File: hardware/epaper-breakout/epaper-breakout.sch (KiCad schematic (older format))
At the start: 59 parts, among them J1 ED097OC4, J2 USB_B_Micro, J3 Conn_01x10, Q1 IRLML6402, SW1 RESET, SW2 BOOT, U1 LT1086-3.3, U2 LT1945, U3 L7915, U4 L7815, U5 ESP32-WROOM-32, U6 CH330N, U7 LM358

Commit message: new copper pour
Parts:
- BOOT1: renamed from SW2; value BOOT -> SW2
- J1: value ED097OC4 -> XF2M-3315-1A; symbol epd_breakout:ED097OC4 -> epd_breakout:XF2M-3315-1A
- J2: value USB_B_Micro -> C10418; symbol Connector:USB_B_Micro -> epd_breakout:C10418
- RESET1: renamed from SW1; value RESET -> SW1
- RXD1: renamed from D6; value RXD -> LED2
- TXD1: renamed from D5; value TXD -> LED1
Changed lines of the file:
@@
 $EndComp
 $Comp
-L epd_breakout:ED097OC4 J1
+L epd_breakout:XF2M-3315-1A J1
 U 1 1 5D6A1D54
 P 9700 1250
 F 0 "J1" H 10350 1893 60  0000 C CNN
-F 1 "ED097OC4" H 10350 1787 60  0000 C CNN
+F 1 "XF2M-3315-1A" H 10350 1787 60  0000 C CNN
 F 2 "epaper-breakout:CONN_ED097OC4" H 10000 1700 60  0000 C CNN
 F 3 "https://datasheet.lcsc.com/szlcsc/Omron-Electronics-XF2M-3315-1A_C231420.pdf" H 9700 1250 60  0001 C CNN
@@
 	7100 3750 7100 3800
 $Comp
-L Switch:SW_Push SW1
+L Switch:SW_Push RESET1
 U 1 1 5D80BDD8
 P 5700 3300
-F 0 "SW1" H 5700 3585 50  0000 C CNN
-F 1 "RESET" H 5700 3494 50  0000 C CNN
+F 0 "RESET1" H 5700 3585 50  0000 C CNN
+F 1 "SW1" H 5700 3494 50  0000 C CNN
 F 2 "epaper-breakout:SW_TS-1187A" H 5700 3500 50  0001 C CNN
 F 3 "https://datasheet.lcsc.com/szlcsc/1901111503_XKB-Enterprise-TS-1187A-B-A-B_C318884.pdf" H 5700 3500 50  0001 C CNN
@@
 $EndComp
 $Comp
-L Connector:USB_B_Micro J2
+L epd_breakout:C10418 J2
 U 1 1 5D83555C
 P 900 6700
 F 0 "J2" H 957 7167 50  0000 C CNN
-F 1 "USB_B_Micro" H 957 7076 50  0000 C CNN
+F 1 "C10418" H 957 7076 50  0000 C CNN
 F 2 "epaper-breakout:USB_Micro-B_A01SB141B1-067" H 1050 6650 50  0001 C CNN
 F 3 "https://lcsc.com/product-detail/USB-Connectors_Jing-Extension-of-the-Electronic-Co-Jing-Extension-of-the-Electronic-Co-MICRO-USB-5S-B-Type-horns-High-temperature_C10418.html" H 1050 6650 50  0001 C CNN
@@
 Connection ~ 5900 3300
 $Comp
-L Switch:SW_Push SW2
+L Switch:SW_Push BOOT1
 U 1 1 5DE2D37B
 P 5700 2600
-F 0 "SW2" H 5700 2885 50  0000 C CNN
-F 1 "BOOT" H 5700 2794 50  0000 C CNN
+F 0 "BOOT1" H 5700 2885 50  0000 C CNN
+F 1 "SW2" H 5700 2794 50  0000 C CNN
 F 2 "epaper-breakout:SW_TS-1187A" H 5700 2800 50  0001 C CNN
 F 3 "https://datasheet.lcsc.com/szlcsc/1901111503_XKB-Enterprise-TS-1187A-B-A-B_C318884.pdf" H 5700 2800 50  0001 C CNN
@@
 	6050 4200 6050 4900
 $Comp
-L Device:LED D6
+L Device:LED RXD1
 U 1 1 5E14B634
 P 5750 4800
-F 0 "D6" V 5800 4700 50  0000 R CNN
-F 1 "RXD" V 5700 4700 50  0000 R CNN
+F 0 "RXD1" V 5800 4750 50  0000 R CNN
+F 1 "LED2" V 5700 4750 50  0000 R CNN
 F 2 "LED_SMD:LED_0805_2012Metric" H 5750 4800 50  0001 C CNN
 F 3 "~" H 5750 4800 50  0001 C CNN
@@
 	0    -1   -1   0
 $EndComp
-$Comp
-L Device:LED D5
+Wire Notes Line
+	5200 4100 5200 5400
+Wire Notes Line
+	5200 5400 7350 5400
+Wire Notes Line
+	7350 5400 7350 4100
+Wire Notes Line
+	5200 4100 7350 4100
+Text Notes 5250 5350 0    50   ~ 0
+Debug
+$Comp
+L Device:LED TXD1
 U 1 1 5E14C380
 P 5600 4800
-F 0 "D5" V 5650 5000 50  0000 R CNN
-F 1 "TXD" V 5550 5000 50  0000 R CNN
+F 0 "TXD1" V 5650 5000 50  0000 R CNN
+F 1 "LED1" V 5550 5050 50  0000 R CNN
 F 2 "LED_SMD:LED_0805_2012Metric" H 5600 4800 50  0001 C CNN
 F 3 "~" H 5600 4800 50  0001 C CNN
@@
 	0    -1   -1   0
 $EndComp
-Wire Notes Line
-	5200 4100 5200 5400
-Wire Notes Line
-	5200 5400 7350 5400
-Wire Notes Line
-	7350 5400 7350 4100
-Wire Notes Line
-	5200 4100 7350 4100
-Text Notes 5250 5350 0    50   ~ 0
-Debug
 $EndSCHEMATC

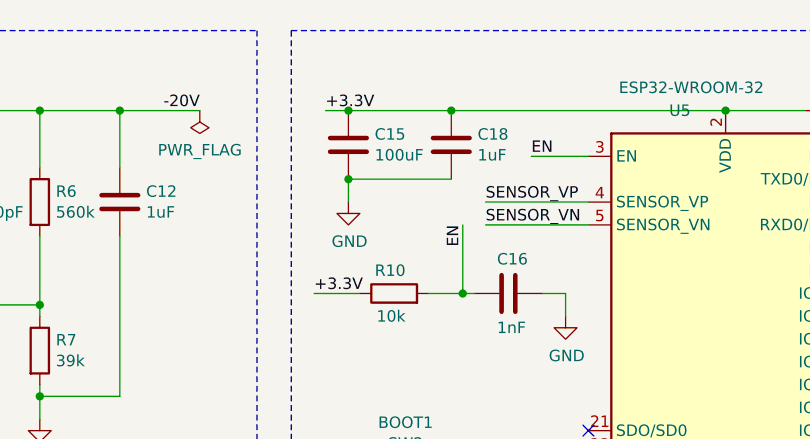
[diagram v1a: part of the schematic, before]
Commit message: lower capacity of C15
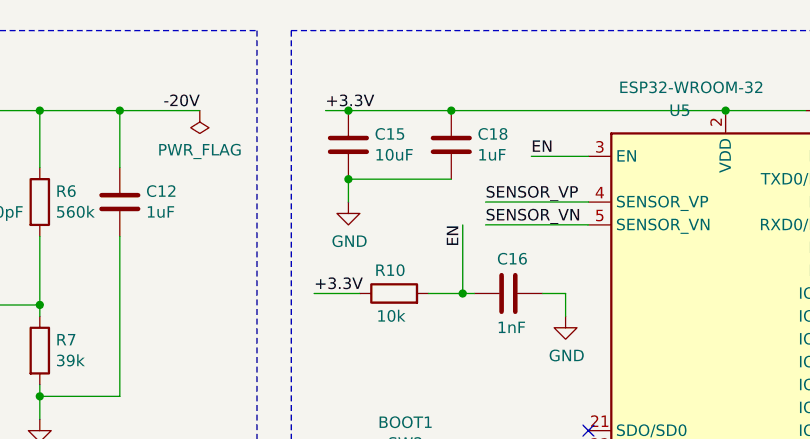
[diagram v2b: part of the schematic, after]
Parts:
- C15: value 100uF -> 10uF; footprint Capacitor_SMD:C_0805_2012Metric -> Capacitor_SMD:C_0603_1608Metric
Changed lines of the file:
@@
 P 5450 1100
 F 0 "C15" H 5565 1146 50  0000 L CNN
-F 1 "100uF" H 5565 1055 50  0000 L CNN
-F 2 "Capacitor_SMD:C_0805_2012Metric" H 5488 950 50  0001 C CNN
+F 1 "10uF" H 5565 1055 50  0000 L CNN
+F 2 "Capacitor_SMD:C_0603_1608Metric" H 5488 950 50  0001 C CNN
 F 3 "~" H 5450 1100 50  0001 C CNN
 	1    5450 1100

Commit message: change to wrover module
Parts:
- removed C19: 1nF, Capacitor_SMD:C_0603_1608Metric, symbol Device:C
- removed J3: Conn_01x10, Connector_PinHeader_2.54mm:PinHeader_1x10_P2.54mm_Vertical, symbol Connector_Generic:Conn_01x10
- removed R17, R18: 1k, Resistor_SMD:R_0805_2012Metric, symbol Device:R
- removed RXD1: LED2, LED_SMD:LED_0805_2012Metric, symbol Device:LED
- removed TXD1: LED1, LED_SMD:LED_0805_2012Metric, symbol Device:LED
- removed U5: ESP32-WROOM-32, RF_Module:ESP32-WROOM-32, symbol RF_Module:ESP32-WROOM-32
- added J3: Conn_02x04_Counter_Clockwise, symbol Connector_Generic:Conn_02x04_Counter_Clockwise
- added U5: ESP32-WROVER, symbol esp32-wrover:ESP32-WROVER
- added U8: 74HC4094-normal, symbol 74HC4094:74HC4094-normal
- C15: value 10uF -> 1nF
- C17: value 1nF -> 10uF
- R12: value 10k -> 470
- R15: value 470 -> 10k
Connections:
- net +3.3V: now also C17.1, R15.2, U5.2 (3V3), U8.15 (OE), U8.16 (VCC); no longer C15.1, J1.30 (UD), R12.1
- net A0: now also J3.7 (Pin_7), U5.6 (IO34)
- net A1: now also J3.8 (Pin_8), U5.7 (IO35)
- net EN: now also C15.2, R12.1, U5.3 (EN); no longer C16.1, R11.1
- net EP_CKH: now also U5.29 (IO5)
- net EP_CKV: now also U5.10 (IO25)
- net EP_D0: now also U5.8 (IO32_XTAL_32K_P)
- net EP_D1: now also U5.9 (IO33_XTAL_32K_N)
- net EP_D2: now also U5.26 (IO4)
- net EP_D3: now also R11.1, R15.1, U5.25 (IO0)
- net EP_D4: now also R13.1, U5.24 (IO2)
- net EP_D5: now also U5.12 (IO27)
- net EP_D6: now also U5.33 (IO21)
- net EP_D7: now also U5.36 (IO22)
- net EP_LE: now also U8.7 (Q3); no longer R13.1
- net EP_MODE: now also U8.6 (Q2); no longer R12.2, R15.1
- net EP_OE: now also U8.4 (Q0)
- net EP_STH: now also U5.11 (IO26)
- net EP_STV: now also U8.5 (Q1)
- net GND: now also C15.1, C16.1, C17.2, U5.1 (GND), U5.15 (GND), U5.38 (GND), U5.39 (GND), U8.8 (GND); no longer C15.2, C16.2, C17.1
- net NEG_CTRL: now also U8.12 (Q6)
- net POS_CTRL: now also U8.13 (Q5)
- net SENSOR_VN: now also J3.6 (Pin_6), U5.5 (SENSOR_VN_IO39)
- net SENSOR_VP: now also J3.5 (Pin_5), U5.4 (SENSOR_VP_IO36)
- net USB_RXD: now also U5.35 (TXD0)
- net USB_TXD: now also U5.34 (RXD0)
- net ~SMPS_CTRL: now also U8.14 (Q4)
- net at BOOT1.2: now also R11.2; no longer R15.2
- new net: U5.30 (IO18), U8.3 (CP)
- new net: U5.31 (IO19), U8.1 (STROBE)
- new net: U5.37 (IO23), U8.2 (DATA)
- new net: C16.2, R12.2, RESET1.2
- new net CS0: J3.1 (Pin_1), U5.23 (IO15)
- new net EP_UD: J1.30 (UD), U8.11 (Q7)
- new net MISO: J3.4 (Pin_4), U5.14 (IO12)
- new net MOSI: J3.2 (Pin_2), U5.16 (IO13)
- new net SCLK: J3.3 (Pin_3), U5.13 (IO14)
- no-connect marks 17 -> 19
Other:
- note removed: "Debug"
- note removed: "ESP32 Module"
- moved on the sheet: J1

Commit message: add second connector, temperature sensor
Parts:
- removed D4: PWR, LED_SMD:LED_0805_2012Metric, symbol Device:LED
- removed J3: Conn_02x04_Counter_Clockwise, symbol Connector_Generic:Conn_02x04_Counter_Clockwise
- removed R16: 1k, Resistor_SMD:R_0805_2012Metric, symbol Device:R
- added J3: Conn_02x05_Counter_Clockwise, Connector_PinHeader_2.54mm:PinHeader_2x05_P2.54mm_Vertical, symbol Connector_Generic:Conn_02x05_Counter_Clockwise
- added J4: ED060SC4, epaper-breakout:HRS_FH26W-39S-0.3SHW(60), symbol ed060sc4:ED060SC4
- added U9: MCP9700AT-ETT, Package_TO_SOT_SMD:SOT-23, symbol Sensor_Temperature:MCP9700AT-ETT
- U5: footprint (none) -> esp32-wrover:ESP32-WROVER
- U8: footprint (none) -> Package_SO:SOIC-16_3.9x9.9mm_P1.27mm
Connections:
- net labels added: V_TEMP
- net labels removed: A1
- wire segments 253 -> 301
